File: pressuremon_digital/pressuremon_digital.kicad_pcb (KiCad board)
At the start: 2 copper layers, 50 x 50 mm, 15 parts, among them J1 Conn_01x04_Pin, J2 Conn_01x04_Pin, J3 Force Config, SW1 SW_SPDT, U3 DS18B20

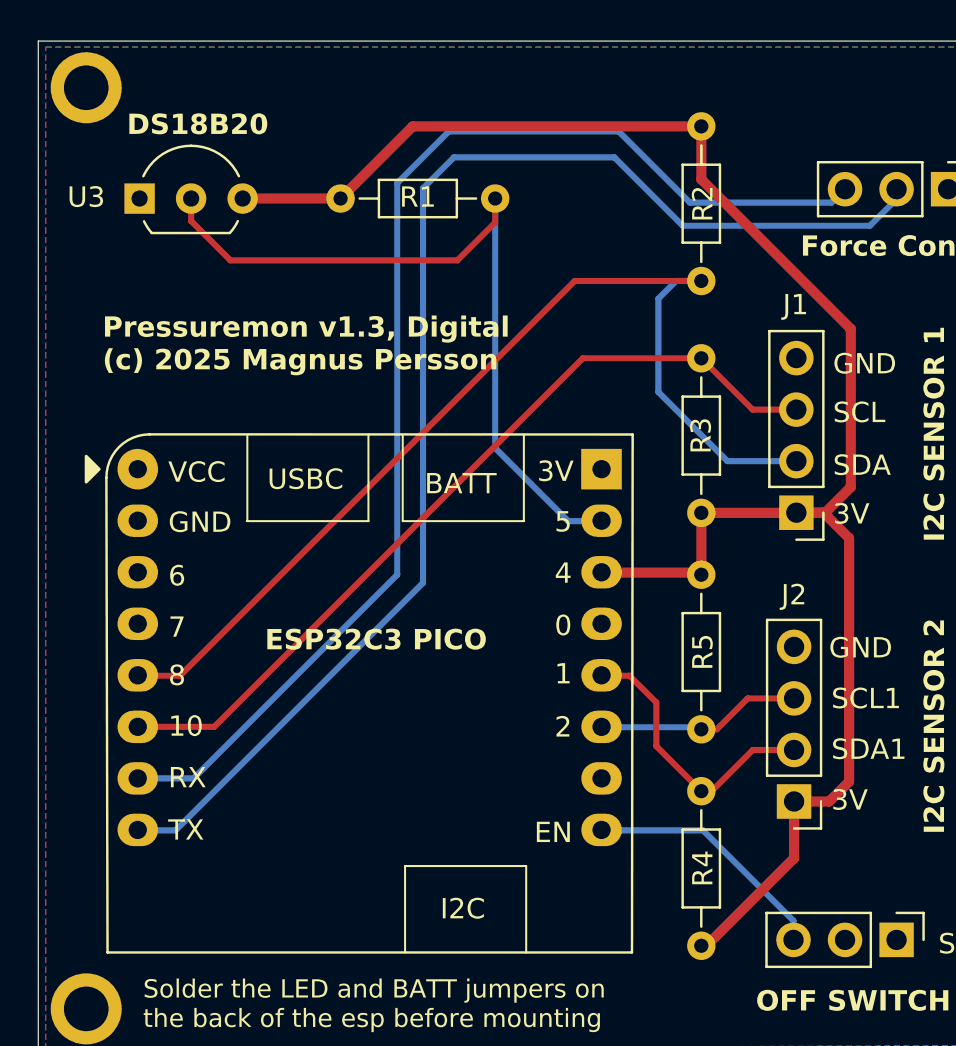
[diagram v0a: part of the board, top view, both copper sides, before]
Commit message: Add resistor values to silkscreen
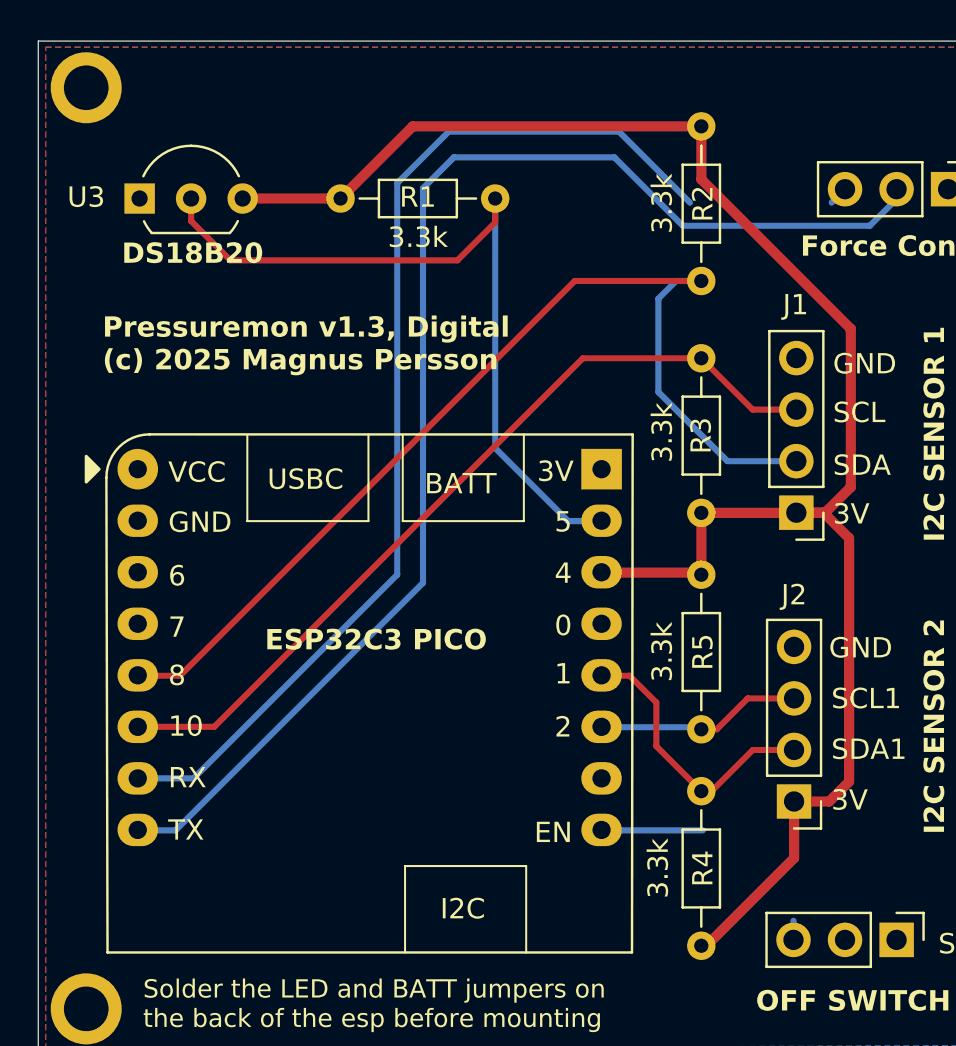
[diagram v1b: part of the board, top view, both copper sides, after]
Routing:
- net Net-(J3-Pin_3): track 61.1 -> 54.1 mm
- net Net-(SW1-C): track 11.6 -> 5.27 mm
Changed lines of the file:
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@@
 			(psa4output no)
 			(plot_black_and_white yes)
-			(plotinvisibletext no)
 			(sketchpadsonfab no)
 			(plotpadnumbers no)
@@
 			(layer "F.Fab")
 		)
-		(fp_text user "${REFERENCE}"
-			(at -2.6 2.4 0)
-			(layer "F.Fab")
-			(effects
-				(font
-					(size 1 1)
-					(thickness 0.15)
-				)
-			)
-		)
 		(pad "1" thru_hole rect
 			(at 0 0 270)
@@
 		(property "Value" "3.3k"
 			(at 3.81 -2.116 90)
-			(layer "F.Fab")
+			(layer "F.SilkS")
 			(effects
 				(font
@@
 			(layer "F.Fab")
 		)
-		(fp_text user "${REFERENCE}"
-			(at 2.4 -0.056 90)
-			(layer "F.Fab")
-			(effects
-				(font
-					(size 1 1)
-					(thickness 0.15)
-				)
-			)
-		)
 		(pad "1" thru_hole rect
 			(at 0 0 180)
@@
 		(property "Value" "3.3k"
 			(at 3.81 1.92 0)
-			(layer "F.Fab")
+			(layer "F.SilkS")
 			(effects
 				(font
@@
 			(layer "F.Fab")
 		)
-		(fp_text user "${REFERENCE}"
-			(at 3.81 -2.06 0)
-			(layer "F.Fab")
-			(effects
-				(font
-					(size 0.72 0.72)
-					(thickness 0.108)
-				)
-			)
-		)
 		(pad "1" thru_hole circle
 			(at 0 0)
@@
 		(property "Value" "3.3k"
 			(at 3.81 1.92 90)
-			(layer "F.Fab")
+			(layer "F.SilkS")
 			(effects
 				(font
@@
 			(at 2.54 2.79 0)
 			(layer "F.Fab")
+			(hide yes)
 			(effects
 				(font
@@
 		(property "Value" "3.3k"
 			(at 3.81 1.92 90)
-			(layer "F.Fab")
+			(layer "F.SilkS")
 			(effects
 				(font
@@
 			(layer "F.Fab")
 		)
-		(fp_text user "${REFERENCE}"
-			(at 3.81 -1.684 90)
-			(layer "F.Fab")
-			(effects
-				(font
-					(size 0.72 0.72)
-					(thickness 0.108)
-				)
-			)
-		)
 		(pad "1" thru_hole circle
 			(at 0 0 270)
@@
 			(layer "F.Fab")
 		)
-		(fp_text user "${REFERENCE}"
-			(at 2.488 -0.022 270)
-			(layer "F.Fab")
-			(effects
-				(font
-					(size 1 1)
-					(thickness 0.15)
-				)
-			)
-		)
 		(pad "1" thru_hole rect
 			(at 0 0 180)
@@
 			)
 		)
-		(fp_text user "${REFERENCE}"
-			(at 10.96 10.94 0)
-			(layer "F.Fab")
-			(effects
-				(font
-					(size 1 1)
-					(thickness 0.15)
-				)
-			)
-		)
 		(pad "1" thru_hole rect
 			(at 22.86 0)
@@
 		(property "Value" "3.3k"
 			(at 3.954 -1.916 90)
-			(layer "F.Fab")
+			(layer "F.SilkS")
 			(effects
 				(font
@@
 			(layer "F.Fab")
 		)
-		(fp_text user "${REFERENCE}"
-			(at 5.154 1.684 90)
-			(layer "F.Fab")
-			(effects
-				(font
-					(size 0.72 0.72)
-					(thickness 0.108)
-				)
-			)
-		)
 		(pad "1" thru_hole circle
 			(at 0 0 90)
@@
 	)
 	(gr_text "DS18B20"
-		(at 112.4 45.2 0)
+		(at 112.15 51.55 0)
 		(layer "F.SilkS")
 		(effects
@@
 	)
 	(segment
-		(start 147.138388 48.461612)
-		(end 140.155612 48.461612)
-		(width 0.3)
-		(layer "B.Cu")
-		(net 11)
-	)
-	(segment
 		(start 125.73 66.802)
 		(end 115.692 76.84)
@@
 		(width 0.3)
 		(layer "B.Cu")
-		(net 12)
-	)
-	(segment
-		(start 140.8 79.4)
-		(end 145.26 83.86)
-		(width 0.3)
-		(layer "B.Cu")
